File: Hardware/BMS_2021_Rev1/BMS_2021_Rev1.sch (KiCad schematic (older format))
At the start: 0 parts

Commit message: Cell filter design finished
need to add resistor values. diodes?
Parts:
- added Conn? (x2): AndersonPP, symbol MRDT_Connectors:AndersonPP
- added Conn?: Molex_SL_09, symbol MRDT_Connectors:Molex_SL_09
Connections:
- new net GND: Conn?.9
- new net cell_1: Conn?.1
- new net cell_2: Conn?.2
- new net cell_3: Conn?.3
- new net cell_4: Conn?.4
- new net cell_5: Conn?.5
- new net cell_6: Conn?.6
- new net cell_7: Conn?.7
- new net cell_8: Conn?.8
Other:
- note added: "BATTERY"
- note added: "change these labels to the other kind\n"
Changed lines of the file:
@@
 $Descr A4 11693 8268
 encoding utf-8
-Sheet 1 2
+Sheet 1 3
 Title ""
 Date ""
@@
 $EndDescr
 $Sheet
-S 500  500  500  500
+S 18000 -3950 500  500
 U 5F7539AB
 F0 "cellFilters" 50
 F1 "cellFilters.sch" 50
 $EndSheet
+$Comp
+L MRDT_Connectors:AndersonPP Conn?
+U 1 1 5F7D577A
+P 600 1650
+F 0 "Conn?" H 808 2037 60  0000 C CNN
+F 1 "AndersonPP" H 808 1931 60  0000 C CNN
+F 2 "" H 450 1100 60  0001 C CNN
+F 3 "" H 450 1100 60  0001 C CNN
+	1    600  1650
+	1    0    0    -1
+$EndComp
+$Comp
+L MRDT_Connectors:AndersonPP Conn?
+U 4 1 5F7D6633
+P 600 1150
+F 0 "Conn?" H 808 1537 60  0000 C CNN
+F 1 "AndersonPP" H 808 1431 60  0000 C CNN
+F 2 "" H 450 600 60  0001 C CNN
+F 3 "" H 450 600 60  0001 C CNN
+	4    600  1150
+	1    0    0    -1
+$EndComp
+$Comp
+L MRDT_Connectors:Molex_SL_09 Conn?
+U 1 1 5F7D732D
+P 750 2050
+F 0 "Conn?" H 692 1863 60  0000 C CNN
+F 1 "Molex_SL_09" H 692 1969 60  0000 C CNN
+F 2 "" H 750 2450 60  0001 C CNN
+F 3 "" H 750 2450 60  0001 C CNN
+	1    750  2050
+	-1   0    0    1
+$EndComp
+Wire Notes Line
+	500  3150 1800 3150
+Wire Notes Line
+	1800 600  500  600
+Wire Notes Line
+	1800 500  1800 3150
+Text Notes 500  600  0    50   ~ 10
+BATTERY
+Text GLabel 1100 2700 2    50   Input ~ 10
+cell_3
+Text GLabel 1100 2900 2    50   Input ~ 10
+cell_1
+Text GLabel 1450 2800 2    50   Input ~ 10
+cell_2
+Text GLabel 1450 2600 2    50   Input ~ 10
+cell_4
+Text GLabel 1100 2500 2    50   Input ~ 10
+cell_5
+Text GLabel 1450 2400 2    50   Input ~ 10
+cell_6
+Text GLabel 1100 2300 2    50   Input ~ 10
+cell_7
+Text GLabel 1450 2200 2    50   Input ~ 10
+cell_8
+Text GLabel 1100 2100 2    50   Input ~ 10
+GND
+Wire Wire Line
+	950  2900 1100 2900
+Wire Wire Line
+	950  2800 1450 2800
+Wire Wire Line
+	950  2700 1100 2700
+Wire Wire Line
+	950  2600 1450 2600
+Wire Wire Line
+	950  2500 1100 2500
+Wire Wire Line
+	950  2400 1450 2400
+Wire Wire Line
+	950  2300 1100 2300
+Wire Wire Line
+	950  2200 1450 2200
+Wire Wire Line
+	950  2100 1100 2100
+$Sheet
+S 2600 600  1250 2550
+U 5F7DC735
+F0 "CELL_FILTERS" 50
+F1 "CELL_FILTERS.sch" 50
+$EndSheet
+Text HLabel 2600 3000 0    50   Input ~ 0
+cell_1
+Text HLabel 2600 2900 0    50   Input ~ 0
+cell_2
+Text HLabel 2600 2800 0    50   Input ~ 0
+cell_3
+Text HLabel 2600 2700 0    50   Input ~ 0
+cell_4
+Text HLabel 2600 2600 0    50   Input ~ 0
+cell_5
+Text HLabel 2600 2500 0    50   Input ~ 0
+cell_6
+Text HLabel 2600 2400 0    50   Input ~ 0
+cell_7
+Text HLabel 2600 2300 0    50   Input ~ 0
+cell_8
+Text HLabel 2600 850  0    50   Input ~ 0
+GND
+Text HLabel 2600 750  0    50   Input ~ 0
+5V+
+Text HLabel 3850 3000 2    50   Output ~ 0
+cell_1_sense
+Text HLabel 3850 2900 2    50   Output ~ 0
+cell_2_sense
+Text HLabel 3850 2800 2    50   Output ~ 0
+cell_3_sense
+Text HLabel 3850 2700 2    50   Output ~ 0
+cell_4_sense
+Text HLabel 3850 2600 2    50   Output ~ 0
+cell_5_sense
+Text HLabel 3850 2500 2    50   Output ~ 0
+cell_6_sense
+Text HLabel 3850 2400 2    50   Output ~ 0
+cell_7_sense
+Text HLabel 3850 2300 2    50   Output ~ 0
+cell_8_sense
+Text Notes 650  3350 0    50   Italic 10
+change these labels to the other kind\n
 $EndSCHEMATC

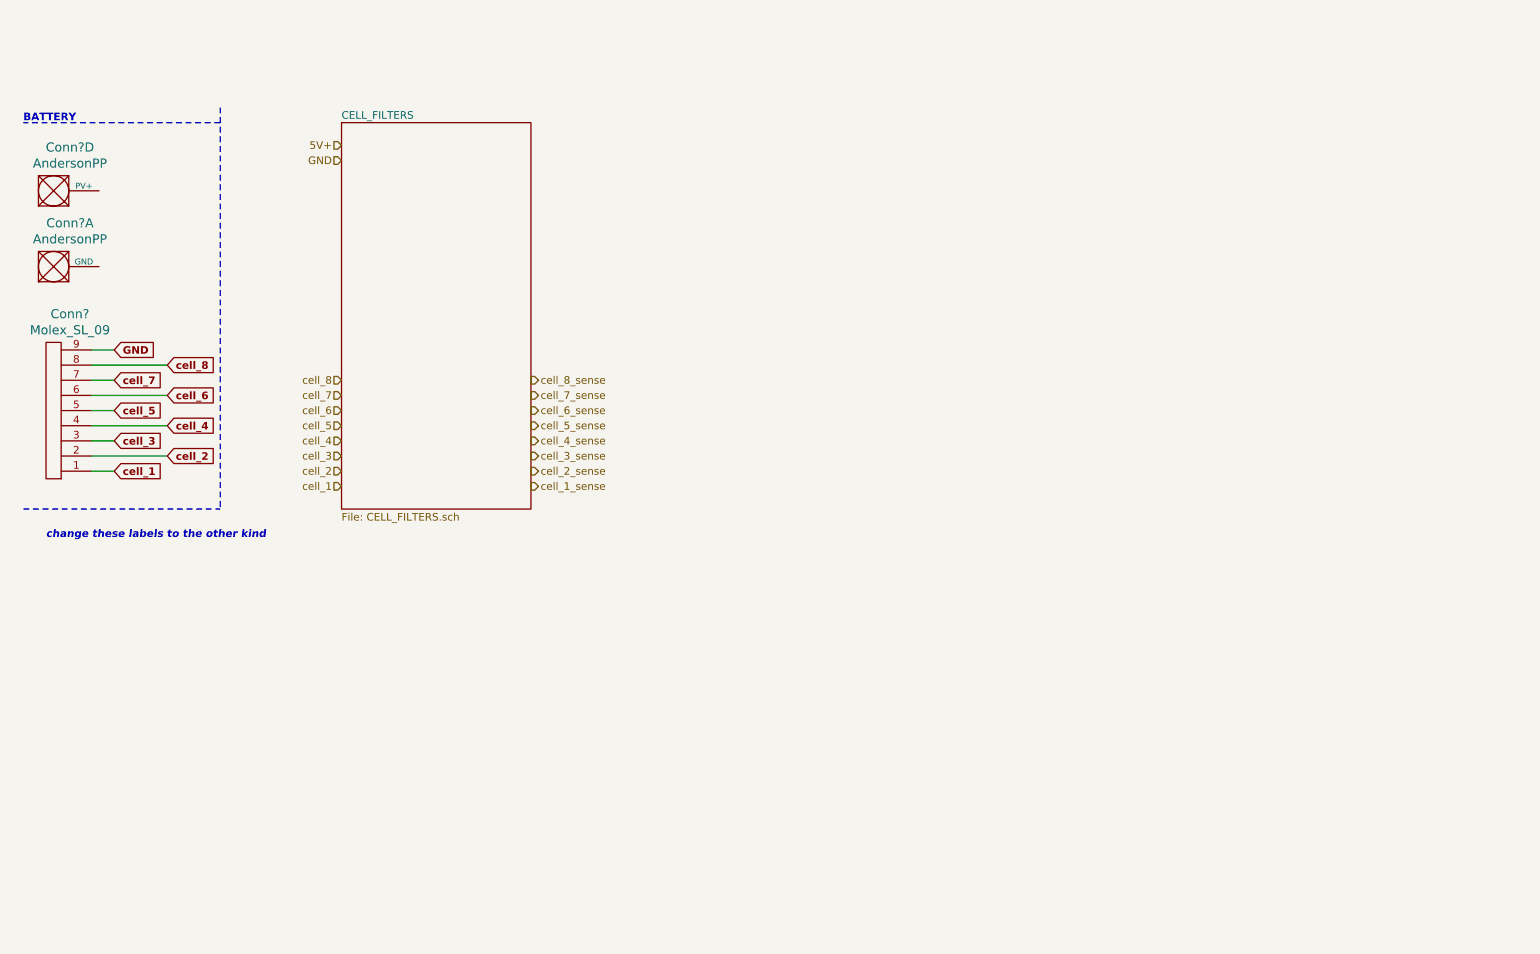
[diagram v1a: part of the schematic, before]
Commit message: TIVA added, current sense WIP
started the current sense circuit. added the tiva layout, need to ask if there is a better way
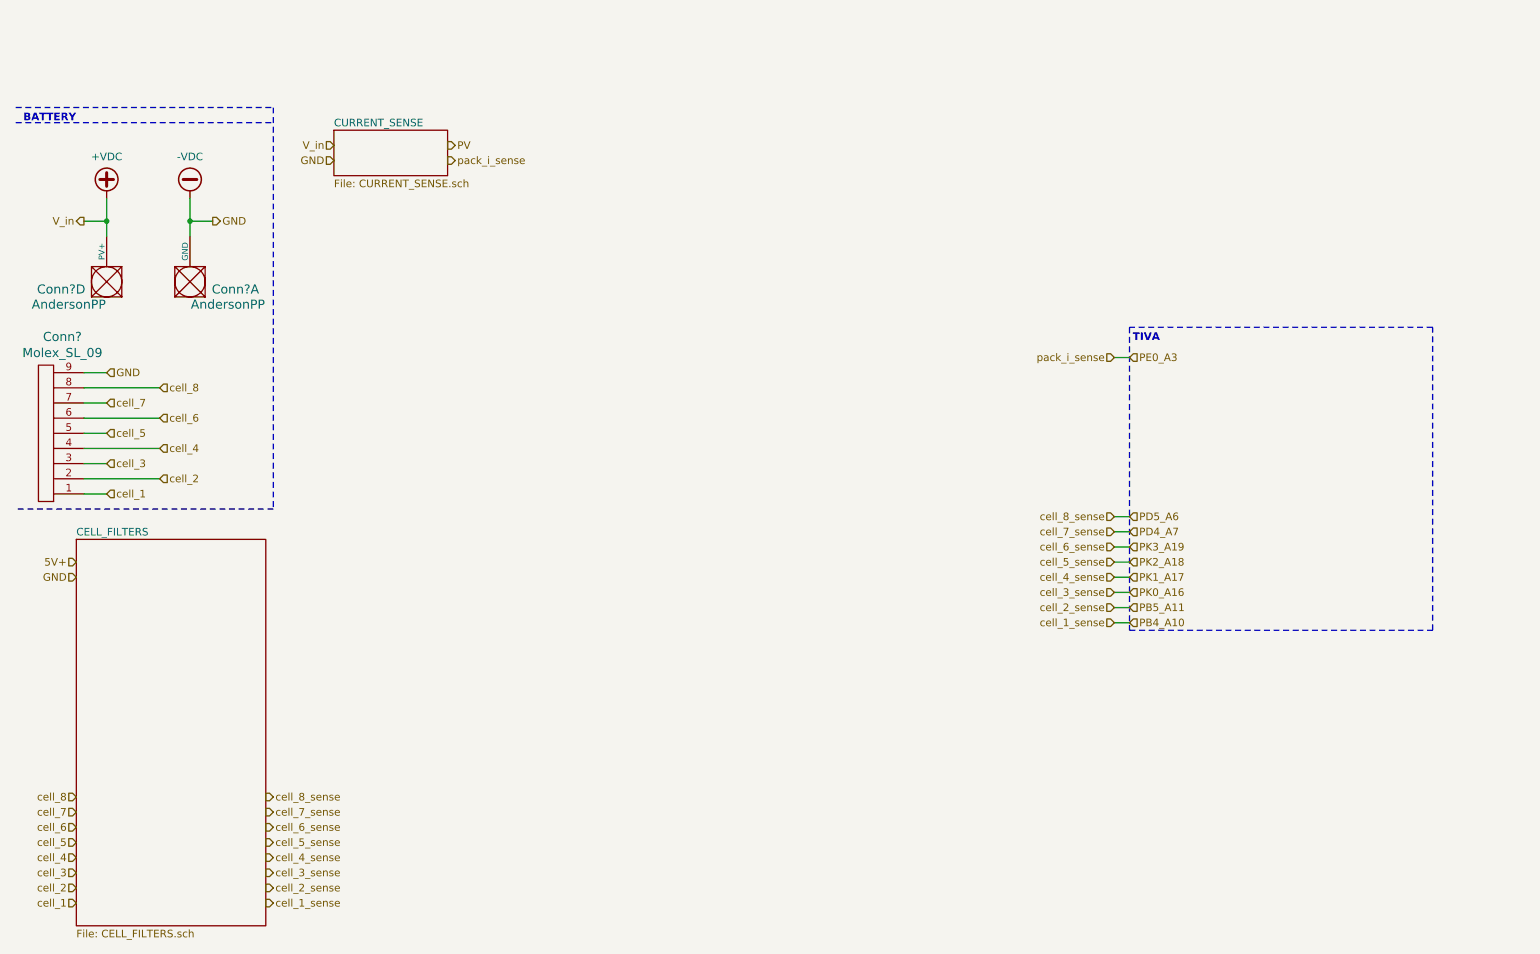
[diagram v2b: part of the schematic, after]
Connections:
- net GND is gone; now on net -VDC: Conn?.9
- net -VDC: now reaches Conn?.1 (GND)
- net +VDC: now reaches Conn?.4 (PV+)
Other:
- note added: "TIVA"
- note removed: "change these labels to the other kind\n"
- moved on the sheet: Conn?, Conn?A, Conn?D
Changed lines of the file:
@@
 $Descr A4 11693 8268
 encoding utf-8
-Sheet 1 3
+Sheet 1 4
 Title ""
 Date ""
@@
 L MRDT_Connectors:AndersonPP Conn?
 U 1 1 5F7D577A
-P 600 1650
-F 0 "Conn?" H 808 2037 60  0000 C CNN
-F 1 "AndersonPP" H 808 1931 60  0000 C CNN
-F 2 "" H 450 1100 60  0001 C CNN
-F 3 "" H 450 1100 60  0001 C CNN
-	1    600  1650
-	1    0    0    -1
+P 1700 1750
+F 0 "Conn?" V 1750 1550 60  0000 C CNN
+F 1 "AndersonPP" V 1650 1600 60  0000 C CNN
+F 2 "" H 1550 1200 60  0001 C CNN
+F 3 "" H 1550 1200 60  0001 C CNN
+	1    1700 1750
+	0    -1   -1   0
 $EndComp
 $Comp
 L MRDT_Connectors:AndersonPP Conn?
 U 4 1 5F7D6633
-P 600 1150
-F 0 "Conn?" H 808 1537 60  0000 C CNN
-F 1 "AndersonPP" H 808 1431 60  0000 C CNN
-F 2 "" H 450 600 60  0001 C CNN
-F 3 "" H 450 600 60  0001 C CNN
-	4    600  1150
-	1    0    0    -1
+P 1150 1750
+F 0 "Conn?" V 1200 2150 60  0000 C CNN
+F 1 "AndersonPP" V 1100 2100 60  0000 C CNN
+F 2 "" H 1000 1200 60  0001 C CNN
+F 3 "" H 1000 1200 60  0001 C CNN
+	4    1150 1750
+	0    -1   -1   0
 $EndComp
 $Comp
 L MRDT_Connectors:Molex_SL_09 Conn?
 U 1 1 5F7D732D
-P 750 2050
-F 0 "Conn?" H 692 1863 60  0000 C CNN
-F 1 "Molex_SL_09" H 692 1969 60  0000 C CNN
-F 2 "" H 750 2450 60  0001 C CNN
-F 3 "" H 750 2450 60  0001 C CNN
-	1    750  2050
+P 700 2200
+F 0 "Conn?" H 642 2013 60  0000 C CNN
+F 1 "Molex_SL_09" H 642 2119 60  0000 C CNN
+F 2 "" H 700 2600 60  0001 C CNN
+F 3 "" H 700 2600 60  0001 C CNN
+	1    700  2200
 	-1   0    0    1
 $EndComp
-Wire Notes Line
-	500  3150 1800 3150
-Wire Notes Line
-	1800 600  500  600
-Wire Notes Line
-	1800 500  1800 3150
 Text Notes 500  600  0    50   ~ 10
 BATTERY
-Text GLabel 1100 2700 2    50   Input ~ 10
+Wire Wire Line
+	900  3050 1050 3050
+Wire Wire Line
+	900  2950 1400 2950
+Wire Wire Line
+	900  2850 1050 2850
+Wire Wire Line
+	900  2750 1400 2750
+Wire Wire Line
+	900  2650 1050 2650
+Wire Wire Line
+	900  2550 1400 2550
+Wire Wire Line
+	900  2450 1050 2450
+Wire Wire Line
+	900  2350 1400 2350
+Wire Wire Line
+	900  2250 1050 2250
+Text HLabel 1050 3050 2    50   Input ~ 0
+cell_1
+Text HLabel 1400 2950 2    50   Input ~ 0
+cell_2
+Text HLabel 1050 2850 2    50   Input ~ 0
 cell_3
-Text GLabel 1100 2900 2    50   Input ~ 10
+Text HLabel 1400 2750 2    50   Input ~ 0
+cell_4
+Text HLabel 1050 2650 2    50   Input ~ 0
+cell_5
+Text HLabel 1400 2550 2    50   Input ~ 0
+cell_6
+Text HLabel 1050 2450 2    50   Input ~ 0
+cell_7
+Text HLabel 1400 2350 2    50   Input ~ 0
+cell_8
+Text HLabel 1050 2250 2    50   Input ~ 0
+GND
+Wire Notes Line
+	7800 1950 7800 3950
+Wire Notes Line
+	7800 3950 9800 3950
+Wire Notes Line
+	9800 3950 9800 1950
+Wire Notes Line
+	9800 1950 7800 1950
+Text Notes 8000 2050 2    50   ~ 10
+TIVA
+Text HLabel 7700 3900 0    50   Input ~ 0
+cell_1_sense
+Text HLabel 7700 3200 0    50   Input ~ 0
+cell_8_sense
+Text HLabel 7700 3300 0    50   Input ~ 0
+cell_7_sense
+Text HLabel 7700 3400 0    50   Input ~ 0
+cell_6_sense
+Text HLabel 7700 3500 0    50   Input ~ 0
+cell_5_sense
+Text HLabel 7700 3600 0    50   Input ~ 0
+cell_4_sense
+Text HLabel 7700 3700 0    50   Input ~ 0
+cell_3_sense
+Text HLabel 7700 3800 0    50   Input ~ 0
+cell_2_sense
+Text HLabel 7800 3900 2    50   Input ~ 0
+PB4_A10
+Text HLabel 7800 3800 2    50   Input ~ 0
+PB5_A11
+Text HLabel 7800 3700 2    50   Input ~ 0
+PK0_A16
+Text HLabel 7800 3600 2    50   Input ~ 0
+PK1_A17
+Text HLabel 7800 3500 2    50   Input ~ 0
+PK2_A18
+Text HLabel 7800 3400 2    50   Input ~ 0
+PK3_A19
+Text HLabel 7800 3300 2    50   Input ~ 0
+PD4_A7
+Text HLabel 7800 3200 2    50   Input ~ 0
+PD5_A6
+Wire Wire Line
+	7700 3200 7800 3200
+Wire Wire Line
+	7700 3300 7800 3300
+Wire Wire Line
+	7700 3400 7800 3400
+Wire Wire Line
+	7700 3500 7800 3500
+Wire Wire Line
+	7700 3600 7800 3600
+Wire Wire Line
+	7700 3700 7800 3700
+Wire Wire Line
+	7700 3800 7800 3800
+Wire Wire Line
+	7700 3900 7800 3900
+Text HLabel 900  1250 0    50   Output ~ 0
+V_in
+Text HLabel 1750 1250 2    50   Output ~ 0
+GND
+Text HLabel 2100 5750 2    50   Output ~ 0
+cell_1_sense
+Text HLabel 850  5750 0    50   Input ~ 0
 cell_1
-Text GLabel 1450 2800 2    50   Input ~ 10
+Text HLabel 850  5650 0    50   Input ~ 0
 cell_2
-Text GLabel 1450 2600 2    50   Input ~ 10
+Text HLabel 850  5550 0    50   Input ~ 0
+cell_3
+Text HLabel 850  5450 0    50   Input ~ 0
 cell_4
-Text GLabel 1100 2500 2    50   Input ~ 10
+Text HLabel 850  5350 0    50   Input ~ 0
 cell_5
-Text GLabel 1450 2400 2    50   Input ~ 10
+Text HLabel 850  5250 0    50   Input ~ 0
 cell_6
-Text GLabel 1100 2300 2    50   Input ~ 10
+Text HLabel 850  5150 0    50   Input ~ 0
 cell_7
-Text GLabel 1450 2200 2    50   Input ~ 10
+Text HLabel 850  5050 0    50   Input ~ 0
 cell_8
-Text GLabel 1100 2100 2    50   Input ~ 10
-GND
-Wire Wire Line
-	950  2900 1100 2900
-Wire Wire Line
-	950  2800 1450 2800
-Wire Wire Line
-	950  2700 1100 2700
-Wire Wire Line
-	950  2600 1450 2600
-Wire Wire Line
-	950  2500 1100 2500
-Wire Wire Line
-	950  2400 1450 2400
-Wire Wire Line
-	950  2300 1100 2300
-Wire Wire Line
-	950  2200 1450 2200
-Wire Wire Line
-	950  2100 1100 2100
+Text HLabel 2100 5050 2    50   Output ~ 0
+cell_8_sense
+Text HLabel 2100 5150 2    50   Output ~ 0
+cell_7_sense
+Text HLabel 2100 5250 2    50   Output ~ 0
+cell_6_sense
+Text HLabel 2100 5350 2    50   Output ~ 0
+cell_5_sense
+Text HLabel 2100 5450 2    50   Output ~ 0
+cell_4_sense
+Text HLabel 2100 5550 2    50   Output ~ 0
+cell_3_sense
+Text HLabel 2100 5650 2    50   Output ~ 0
+cell_2_sense
+Text HLabel 850  3500 0    50   Input ~ 0
+5V+
+Text HLabel 850  3600 0    50   Input ~ 0
+GND
+Wire Notes Line
+	450  600  2150 600
+Wire Notes Line
+	450  500  2150 500
+$Comp
+L power:+VDC #PWR?
+U 1 1 5F80802A
+P 1050 1100
+F 0 "#PWR?" H 1050 1000 50  0001 C CNN
+F 1 "+VDC" H 1050 1375 50  0000 C CNN
+F 2 "" H 1050 1100 50  0001 C CNN
+F 3 "" H 1050 1100 50  0001 C CNN
+	1    1050 1100
+	1    0    0    -1
+$EndComp
+$Comp
+L power:-VDC #PWR?
+U 1 1 5F8089AD
+P 1600 1100
+F 0 "#PWR?" H 1600 1000 50  0001 C CNN
+F 1 "-VDC" H 1600 1375 50  0000 C CNN
+F 2 "" H 1600 1100 50  0001 C CNN
+F 3 "" H 1600 1100 50  0001 C CNN
+	1    1600 1100
+	1    0    0    -1
+$EndComp
+Wire Wire Line
+	1050 1100 1050 1250
+Wire Wire Line
+	900  1250 1050 1250
+Connection ~ 1050 1250
+Wire Wire Line
+	1050 1250 1050 1350
+Wire Wire Line
+	1600 1100 1600 1250
+Wire Wire Line
+	1600 1250 1750 1250
+Connection ~ 1600 1250
+Wire Wire Line
+	1600 1250 1600 1350
+Wire Notes Line
+	2150 500  2150 3150
+Wire Notes Line
+	2150 3150 450  3150
+Text HLabel 2550 750  0    50   Input ~ 0
+V_in
+Text HLabel 2550 850  0    50   Input ~ 0
+GND
 $Sheet
-S 2600 600  1250 2550
+S 850  3350 1250 2550
 U 5F7DC735
 F0 "CELL_FILTERS" 50
 F1 "CELL_FILTERS.sch" 50
 $EndSheet
-Text HLabel 2600 3000 0    50   Input ~ 0
-cell_1
-Text HLabel 2600 2900 0    50   Input ~ 0
-cell_2
-Text HLabel 2600 2800 0    50   Input ~ 0
-cell_3
-Text HLabel 2600 2700 0    50   Input ~ 0
-cell_4
-Text HLabel 2600 2600 0    50   Input ~ 0
-cell_5
-Text HLabel 2600 2500 0    50   Input ~ 0
-cell_6
-Text HLabel 2600 2400 0    50   Input ~ 0
-cell_7
-Text HLabel 2600 2300 0    50   Input ~ 0
-cell_8
-Text HLabel 2600 850  0    50   Input ~ 0
-GND
-Text HLabel 2600 750  0    50   Input ~ 0
-5V+
-Text HLabel 3850 3000 2    50   Output ~ 0
-cell_1_sense
-Text HLabel 3850 2900 2    50   Output ~ 0
-cell_2_sense
-Text HLabel 3850 2800 2    50   Output ~ 0
-cell_3_sense
-Text HLabel 3850 2700 2    50   Output ~ 0
-cell_4_sense
-Text HLabel 3850 2600 2    50   Output ~ 0
-cell_5_sense
-Text HLabel 3850 2500 2    50   Output ~ 0
-cell_6_sense
-Text HLabel 3850 2400 2    50   Output ~ 0
-cell_7_sense
-Text HLabel 3850 2300 2    50   Output ~ 0
-cell_8_sense
-Text Notes 650  3350 0    50   Italic 10
-change these labels to the other kind\n
+$Sheet
+S 2550 650  750  300
+U 5F80E1AD
+F0 "CURRENT_SENSE" 50
+F1 "CURRENT_SENSE.sch" 50
+$EndSheet
+Text HLabel 3300 750  2    50   Output ~ 0
+PV
+Text HLabel 3300 850  2    50   Output ~ 0
+pack_i_sense
+Text HLabel 7700 2150 0    50   Input ~ 0
+pack_i_sense
+Text HLabel 7800 2150 2    50   Input ~ 0
+PE0_A3
+Wire Wire Line
+	7700 2150 7800 2150
 $EndSCHEMATC

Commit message: built current sensing circuit, added heierarchical sheets for other circuits
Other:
- note added: "ENTER RESISTOR VALUES\n"
- note added: "not done"
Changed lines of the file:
@@
 EELAYER 30 0
 EELAYER END
-$Descr A4 11693 8268
+$Descr USLetter 11000 8500
 encoding utf-8
-Sheet 1 4
+Sheet 1 10
 Title ""
 Date ""
@@
 Comment4 ""
 $EndDescr
-$Sheet
-S 18000 -3950 500  500
-U 5F7539AB
-F0 "cellFilters" 50
-F1 "cellFilters.sch" 50
-$EndSheet
 $Comp
 L MRDT_Connectors:AndersonPP Conn?
@@
 Wire Notes Line
 	2150 3150 450  3150
-Text HLabel 2550 750  0    50   Input ~ 0
+Text HLabel 2550 700  0    50   Input ~ 0
 V_in
-Text HLabel 2550 850  0    50   Input ~ 0
+Text HLabel 2550 900  0    50   Input ~ 0
 GND
 $Sheet
@@
 Wire Wire Line
 	7700 2150 7800 2150
+$Sheet
+S 2550 1350 750  300
+U 5F7FDD72
+F0 "5V_BUCK" 50
+F1 "5V_BUCK.sch" 50
+$EndSheet
+Text HLabel 2550 1450 0    50   Input ~ 0
+PV
+Text HLabel 2550 1550 0    50   Input ~ 0
+GND
+Text HLabel 3300 1500 2    50   Output ~ 0
+5V
+Text HLabel 2550 2150 0    50   Input ~ 0
+PV
+Text HLabel 2550 2250 0    50   Input ~ 0
+GND
+Text HLabel 3300 2200 2    50   Output ~ 0
+3V3
+$Sheet
+S 2550 2050 750  300
+U 5F7FE1CA
+F0 "3V3_BUCK" 50
+F1 "3V3_BUCK.sch" 50
+$EndSheet
+Text Notes 3550 1500 0    50   ~ 0
+not done
+Text Notes 3600 2250 0    50   ~ 0
+not done
+$Sheet
+S 2550 2650 1200 850
+U 5F801232
+F0 "ESTOP" 50
+F1 "ESTOP.sch" 50
+$EndSheet
+$Sheet
+S 2550 3850 1200 850
+U 5F80136E
+F0 "LOGIC_SWITCH" 50
+F1 "LOGIC_SWITCH.sch" 50
+$EndSheet
+Text Notes 3850 3100 0    50   ~ 0
+not done
+Text Notes 3800 4300 0    50   ~ 0
+not done
+$Sheet
+S 4400 1350 750  300
+U 5F803423
+F0 "sheet5F80341A" 50
+F1 "5V_BUCK.sch" 50
+$EndSheet
+$Sheet
+S 4400 2050 750  300
+U 5F80342B
+F0 "sheet5F80341B" 50
+F1 "3V3_BUCK.sch" 50
+$EndSheet
+Text Notes 5400 1500 0    50   ~ 0
+not done
+Text Notes 5450 2250 0    50   ~ 0
+not done
+Text HLabel 2550 800  0    50   Input ~ 0
+5V
+Text Notes 5400 800  0    50   ~ 0
+not done
+$Sheet
+S 4400 650  750  300
+U 5F80341F
+F0 "FANS" 50
+F1 "FANS.sch" 50
+$EndSheet
+Text Notes 1100 6350 0    50   ~ 0
+ENTER RESISTOR VALUES\n
 $EndSCHEMATC
